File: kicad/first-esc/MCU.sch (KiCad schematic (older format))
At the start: 12 parts

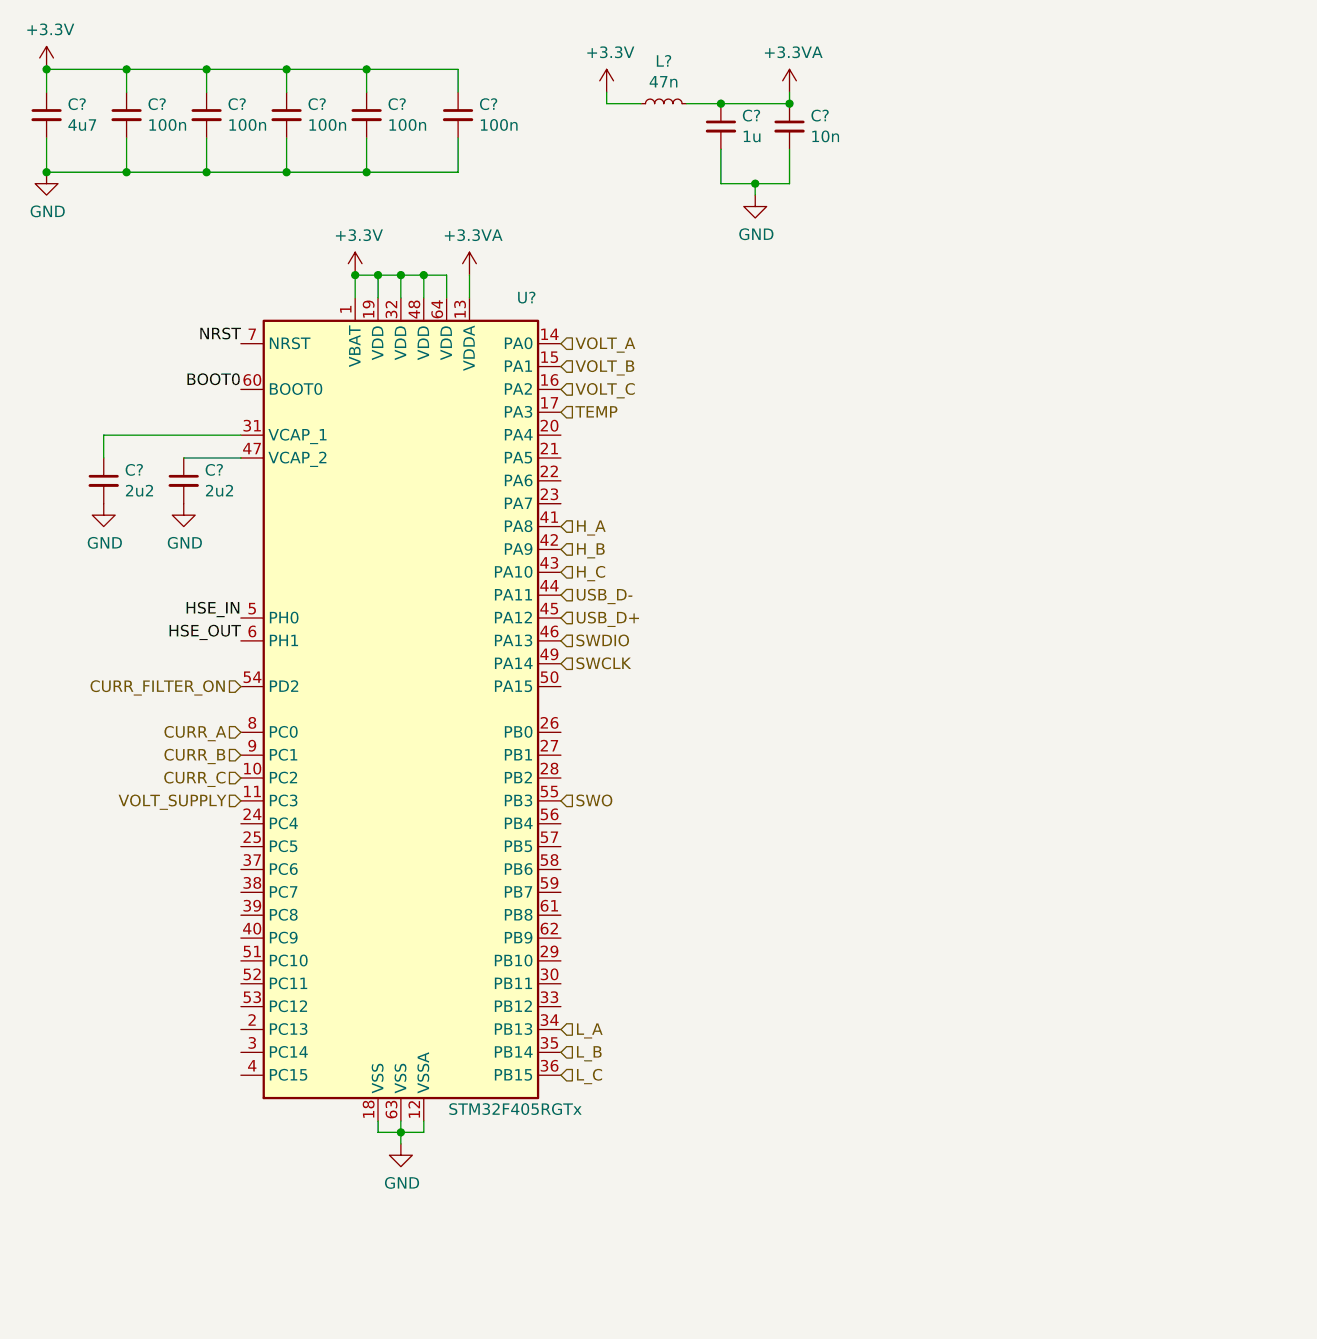
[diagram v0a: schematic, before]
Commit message: (hopefully) finishing up PCB schematic
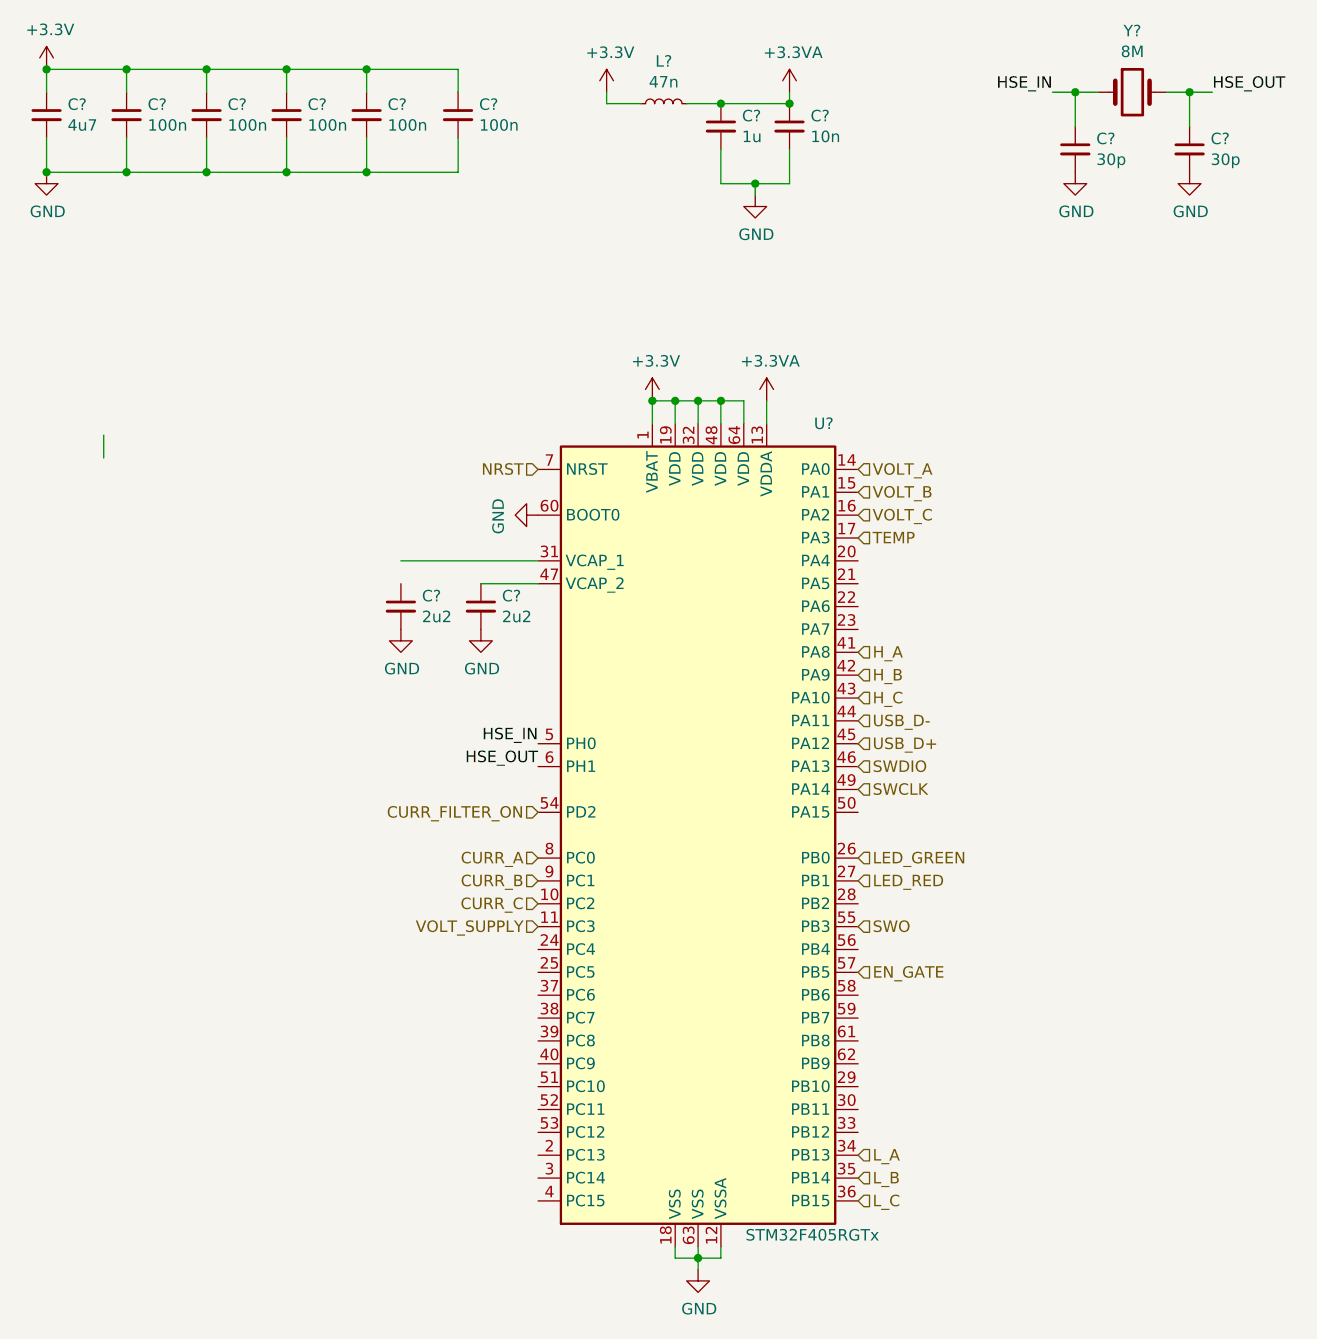
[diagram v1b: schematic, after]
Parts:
- added C? (x2): 30p, symbol Device:C_Small
- added Y?: 8M, symbol Device:Crystal
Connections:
- net labels added: EN_GATE, LED_GREEN, LED_RED
- net labels removed: BOOT0
- wire segments 51 -> 57
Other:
- moved on the sheet: C?, U?

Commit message: mostly finished schematic, started PCB layout
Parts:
- C40, C41, C42, C43, C44, C45, C46, C47, C48, C49, C50, C51: renamed from C?; footprint (none) -> Capacitor_SMD:C_0603_1608Metric
- L2: renamed from L?; footprint (none) -> Inductor_SMD:L_0805_2012Metric
- Y1: renamed from Y?; footprint (none) -> Crystal:Crystal_SMD_5032-2Pin_5.0x3.2mm
- gave numbers to parts that had none: 1
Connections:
- net labels added: JTDI
